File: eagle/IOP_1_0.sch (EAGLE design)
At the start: 14 parts, among them X1 A, X2 B

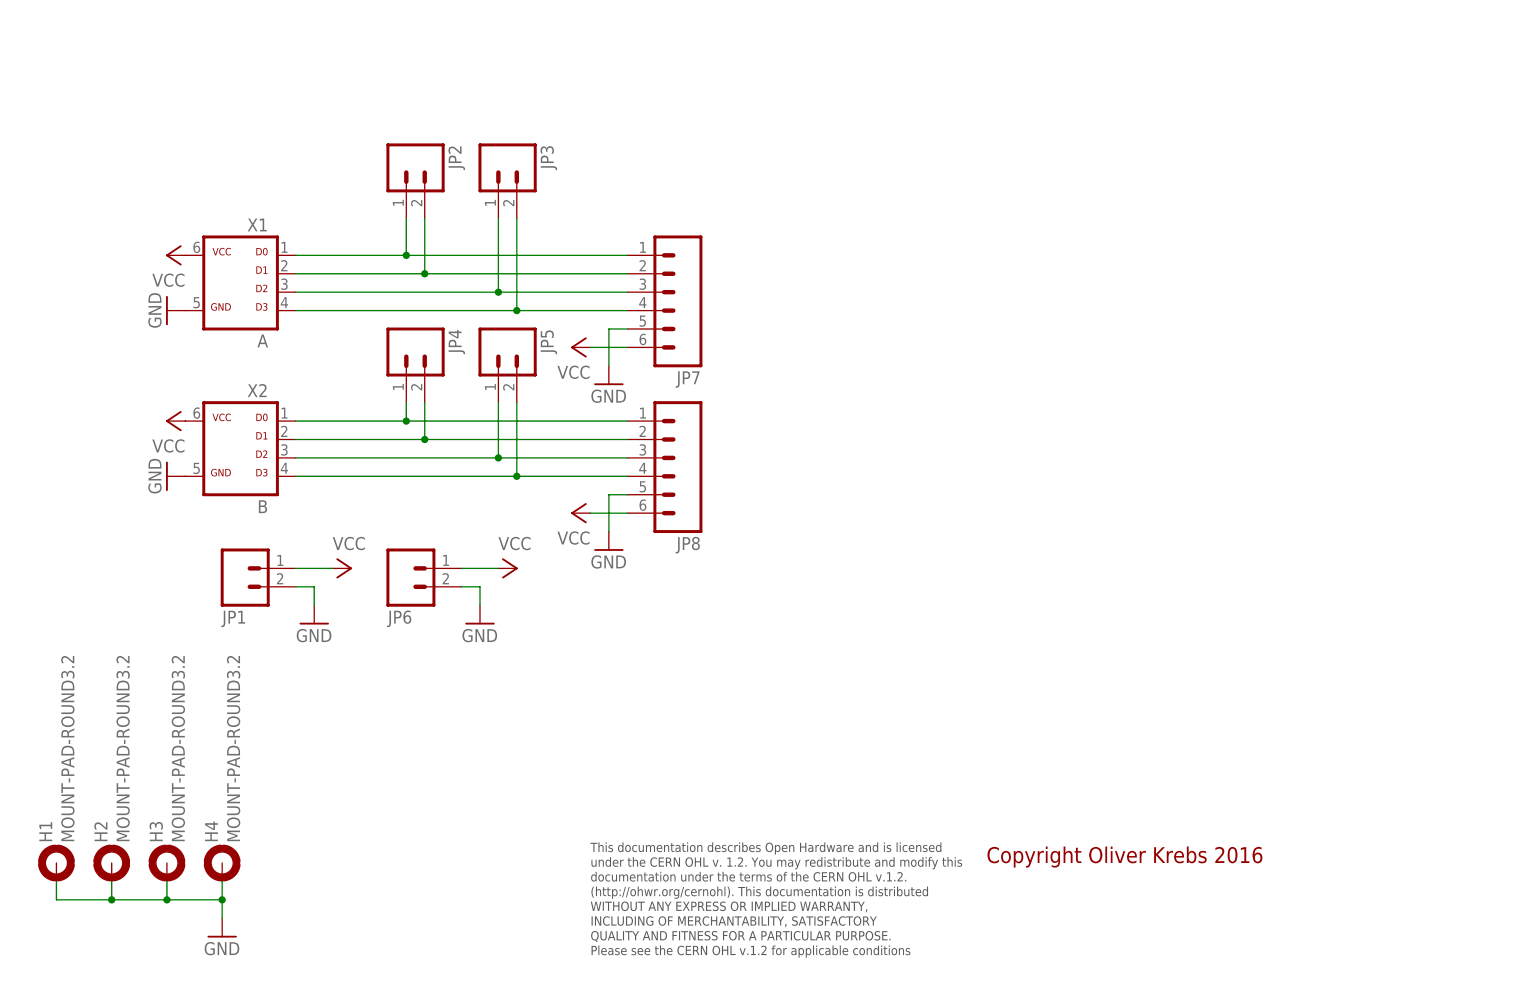
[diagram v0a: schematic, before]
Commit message: Add new tetra-Board and arduino files
Add AMP_1_0, AVC_1_0, D18_1_1, IOP_1_2, MIC_1_0, PIN_1_1, POT_1_0, PWA_1_0, PWR_1_0, RGF 2.0, SOC_2_0, VLT_1_0
Add mex_nano_shield_keyboard, mex_nano_shied_numbers

New arduino projects
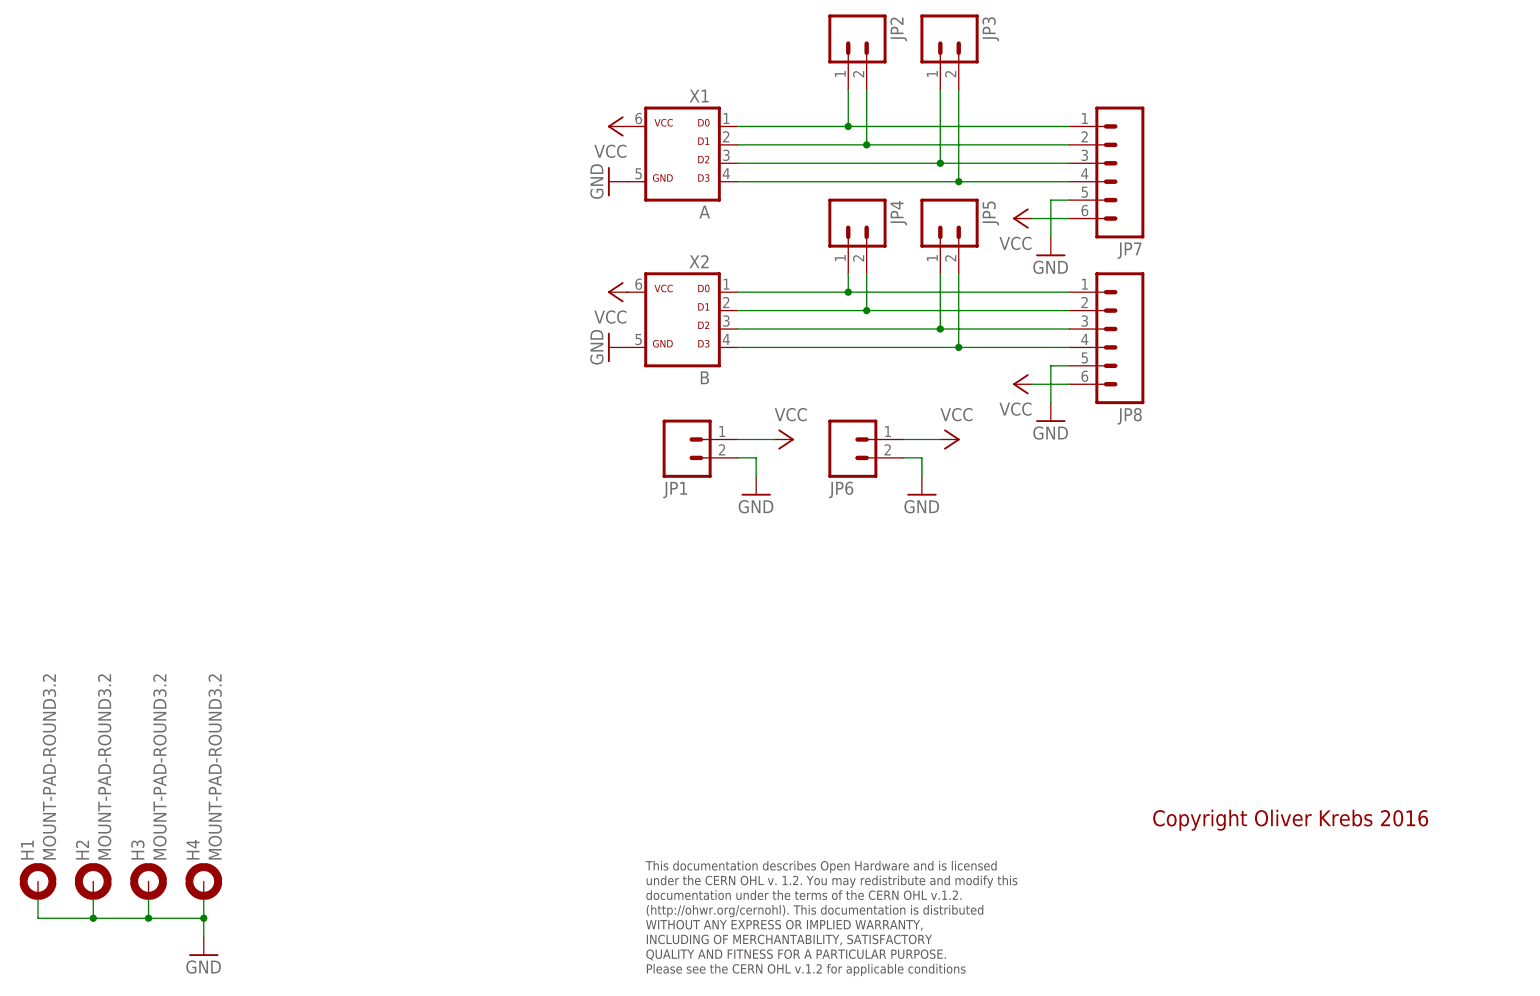
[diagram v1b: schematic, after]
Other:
- moved on the sheet: H1, H2, H3, H4, JP1, JP2, JP3, JP4, JP5, JP6, JP7, JP8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
